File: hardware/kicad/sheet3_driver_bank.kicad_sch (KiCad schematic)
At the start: 32 parts, among them U101 TC4427ACOA, U102 TC4427ACOA, U103 TC4427ACOA, U104 TC4427ACOA, U105 TC4427ACOA, U106 TC4427ACOA, U107 TC4427ACOA, U108 TC4427ACOA, U109 TC4427ACOA, U110 TC4427ACOA, U111 TC4427ACOA, U112 TC4427ACOA, U113 TC4427ACOA, U114 TC4427ACOA, U115 TC4427ACOA, U116 TC4427ACOA, U117 TC4427ACOA, U118 TC4427ACOA, U119 TC4427ACOA, U120 TC4427ACOA, U121 TC4427ACOA, U122 TC4427ACOA, U123 TC4427ACOA, U124 TC4427ACOA, U125 TC4427ACOA, U126 TC4427ACOA, U127 TC4427ACOA, U128 TC4427ACOA, U129 TC4427ACOA, U130 TC4427ACOA, U131 TC4427ACOA, U132 TC4427ACOA

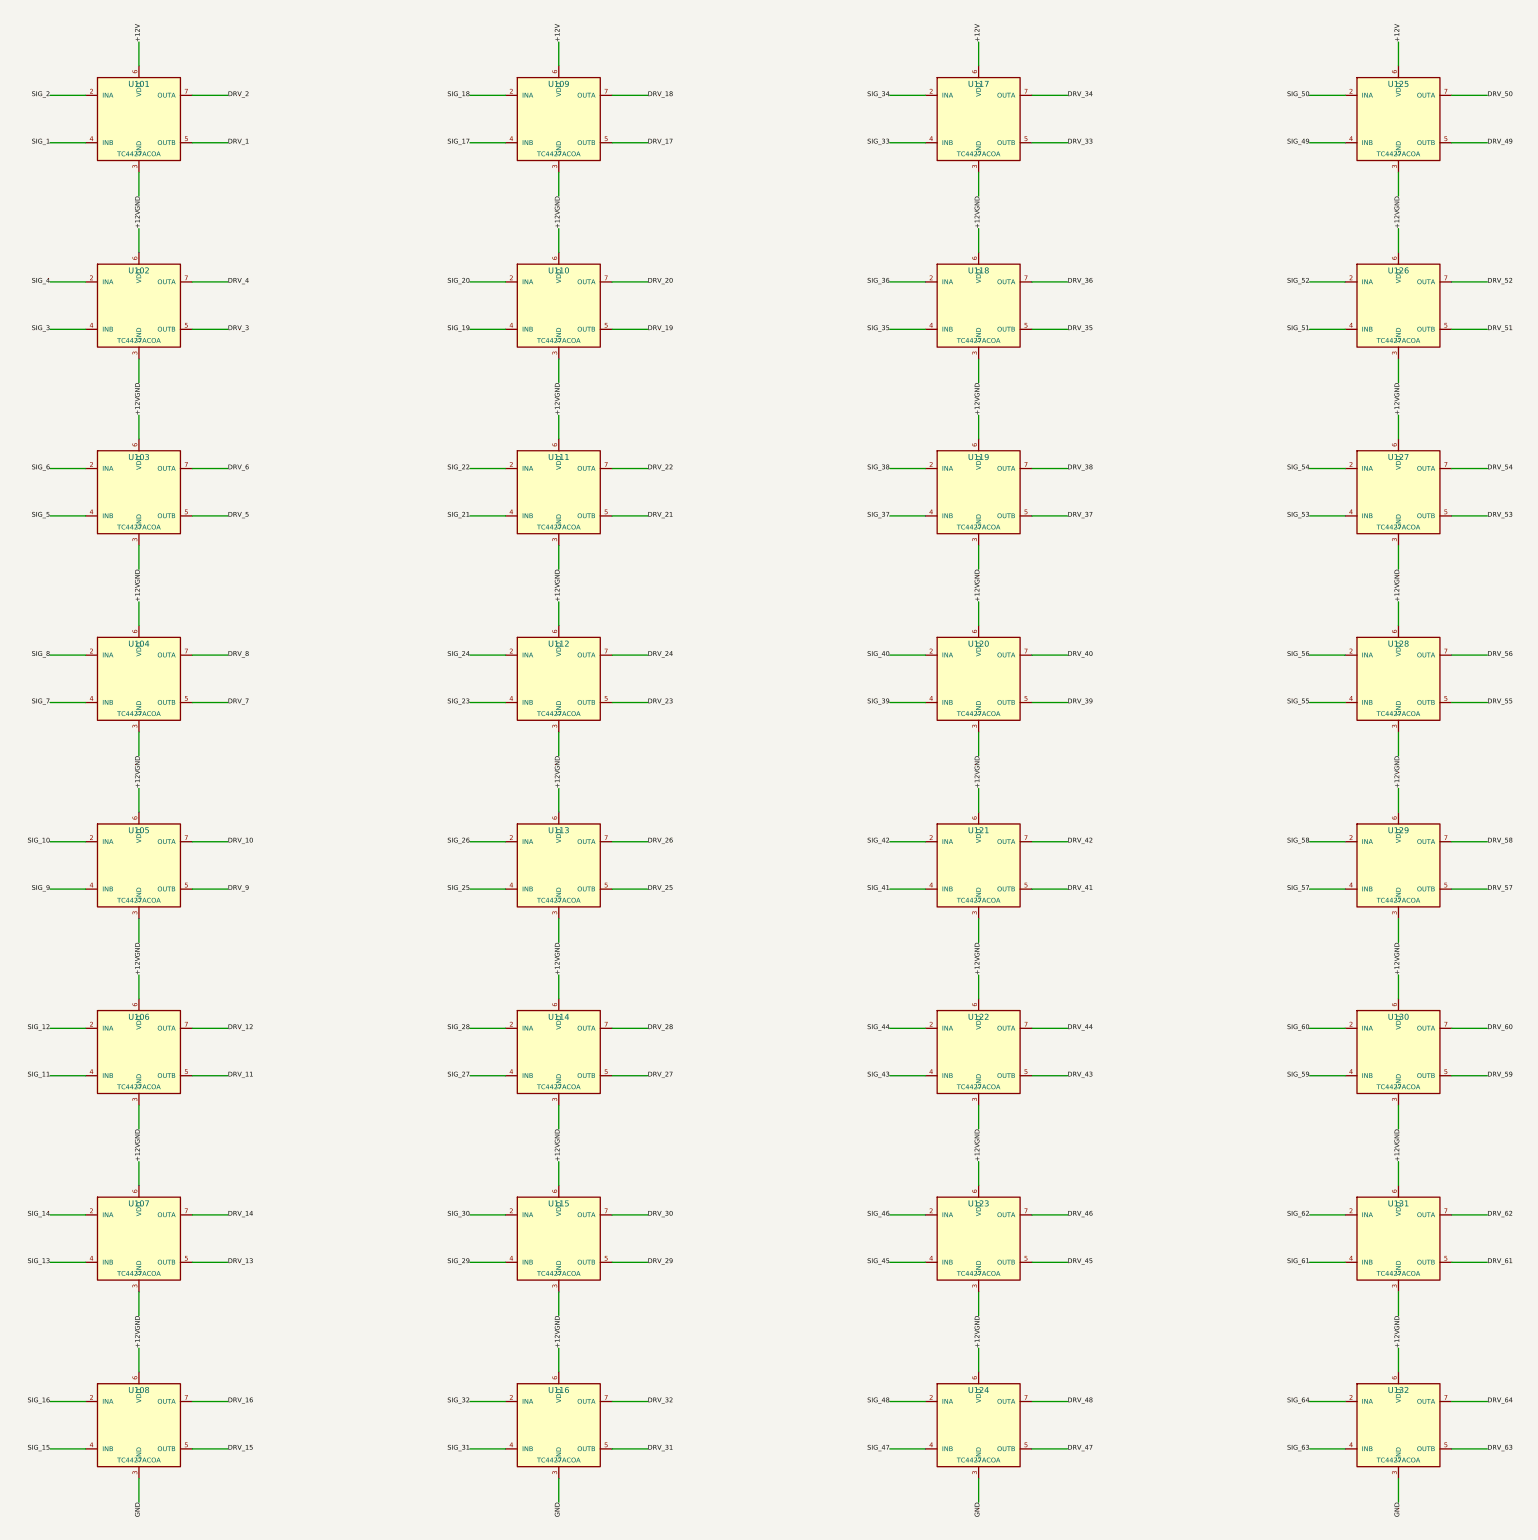
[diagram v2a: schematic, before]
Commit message: Update KiCad symbols and netlist for spotless F8 PCB sync
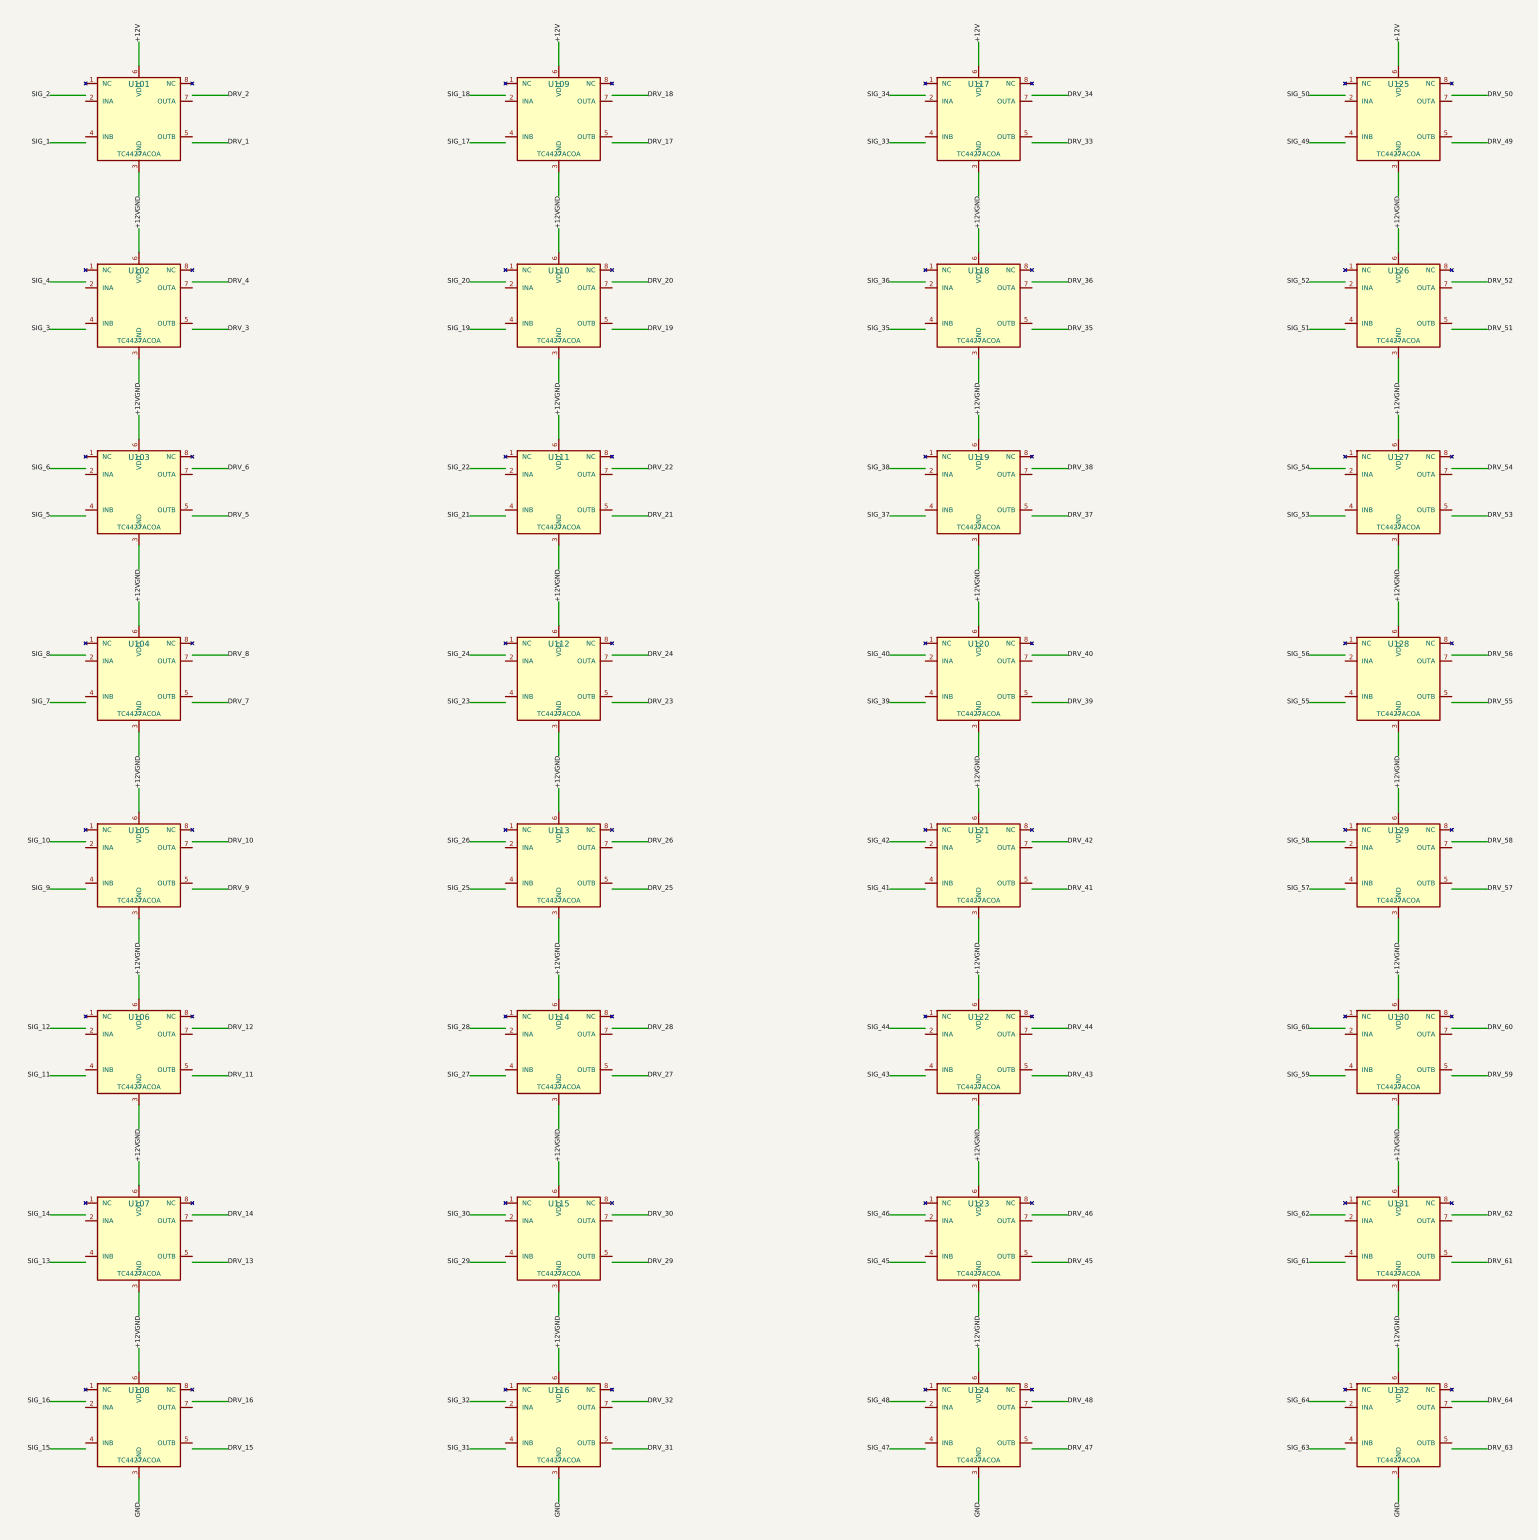
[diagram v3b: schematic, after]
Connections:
- net DRV_1: no longer U101.5 (OUTB)
- net DRV_10: no longer U105.7 (OUTA)
- net DRV_11: no longer U106.5 (OUTB)
- net DRV_12: no longer U106.7 (OUTA)
- net DRV_13: no longer U107.5 (OUTB)
- net DRV_14: no longer U107.7 (OUTA)
- net DRV_15: no longer U108.5 (OUTB)
- net DRV_16: no longer U108.7 (OUTA)
- net DRV_17: no longer U109.5 (OUTB)
- net DRV_18: no longer U109.7 (OUTA)
- net DRV_19: no longer U110.5 (OUTB)
- net DRV_2: no longer U101.7 (OUTA)
- net DRV_20: no longer U110.7 (OUTA)
- net DRV_21: no longer U111.5 (OUTB)
- net DRV_22: no longer U111.7 (OUTA)
- net DRV_23: no longer U112.5 (OUTB)
- net DRV_24: no longer U112.7 (OUTA)
- net DRV_25: no longer U113.5 (OUTB)
- net DRV_26: no longer U113.7 (OUTA)
- net DRV_27: no longer U114.5 (OUTB)
- net DRV_28: no longer U114.7 (OUTA)
- net DRV_29: no longer U115.5 (OUTB)
- net DRV_3: no longer U102.5 (OUTB)
- net DRV_30: no longer U115.7 (OUTA)
- net DRV_31: no longer U116.5 (OUTB)
- net DRV_32: no longer U116.7 (OUTA)
- net DRV_33: no longer U117.5 (OUTB)
- net DRV_34: no longer U117.7 (OUTA)
- net DRV_35: no longer U118.5 (OUTB)
- net DRV_36: no longer U118.7 (OUTA)
- net DRV_37: no longer U119.5 (OUTB)
- net DRV_38: no longer U119.7 (OUTA)
- net DRV_39: no longer U120.5 (OUTB)
- net DRV_4: no longer U102.7 (OUTA)
- net DRV_40: no longer U120.7 (OUTA)
- net DRV_41: no longer U121.5 (OUTB)
- net DRV_42: no longer U121.7 (OUTA)
- net DRV_43: no longer U122.5 (OUTB)
- net DRV_44: no longer U122.7 (OUTA)
- net DRV_45: no longer U123.5 (OUTB)
- net DRV_46: no longer U123.7 (OUTA)
- net DRV_47: no longer U124.5 (OUTB)
- net DRV_48: no longer U124.7 (OUTA)
- net DRV_49: no longer U125.5 (OUTB)
- net DRV_5: no longer U103.5 (OUTB)
- net DRV_50: no longer U125.7 (OUTA)
- net DRV_51: no longer U126.5 (OUTB)
- net DRV_52: no longer U126.7 (OUTA)
- net DRV_53: no longer U127.5 (OUTB)
- net DRV_54: no longer U127.7 (OUTA)
- net DRV_55: no longer U128.5 (OUTB)
- net DRV_56: no longer U128.7 (OUTA)
- net DRV_57: no longer U129.5 (OUTB)
- net DRV_58: no longer U129.7 (OUTA)
- net DRV_59: no longer U130.5 (OUTB)
- net DRV_6: no longer U103.7 (OUTA)
- net DRV_60: no longer U130.7 (OUTA)
- net DRV_61: no longer U131.5 (OUTB)
- net DRV_62: no longer U131.7 (OUTA)
- net DRV_63: no longer U132.5 (OUTB)
- net DRV_64: no longer U132.7 (OUTA)
- net DRV_7: no longer U104.5 (OUTB)
- net DRV_8: no longer U104.7 (OUTA)
- net DRV_9: no longer U105.5 (OUTB)
- net SIG_1: no longer U101.4 (INB)
- net SIG_10: no longer U105.2 (INA)
- net SIG_11: no longer U106.4 (INB)
- net SIG_12: no longer U106.2 (INA)
- net SIG_13: no longer U107.4 (INB)
- net SIG_14: no longer U107.2 (INA)
- net SIG_15: no longer U108.4 (INB)
- net SIG_16: no longer U108.2 (INA)
- net SIG_17: no longer U109.4 (INB)
- net SIG_18: no longer U109.2 (INA)
- net SIG_19: no longer U110.4 (INB)
- net SIG_2: no longer U101.2 (INA)
- net SIG_20: no longer U110.2 (INA)
- net SIG_21: no longer U111.4 (INB)
- net SIG_22: no longer U111.2 (INA)
- net SIG_23: no longer U112.4 (INB)
- net SIG_24: no longer U112.2 (INA)
- net SIG_25: no longer U113.4 (INB)
- net SIG_26: no longer U113.2 (INA)
- net SIG_27: no longer U114.4 (INB)
- net SIG_28: no longer U114.2 (INA)
- net SIG_29: no longer U115.4 (INB)
- net SIG_3: no longer U102.4 (INB)
- net SIG_30: no longer U115.2 (INA)
- net SIG_31: no longer U116.4 (INB)
- net SIG_32: no longer U116.2 (INA)
- net SIG_33: no longer U117.4 (INB)
- net SIG_34: no longer U117.2 (INA)
- net SIG_35: no longer U118.4 (INB)
- net SIG_36: no longer U118.2 (INA)
- net SIG_37: no longer U119.4 (INB)
- net SIG_38: no longer U119.2 (INA)
- net SIG_39: no longer U120.4 (INB)
- net SIG_4: no longer U102.2 (INA)
- net SIG_40: no longer U120.2 (INA)
- net SIG_41: no longer U121.4 (INB)
- net SIG_42: no longer U121.2 (INA)
- net SIG_43: no longer U122.4 (INB)
- net SIG_44: no longer U122.2 (INA)
- net SIG_45: no longer U123.4 (INB)
- net SIG_46: no longer U123.2 (INA)
- net SIG_47: no longer U124.4 (INB)
- net SIG_48: no longer U124.2 (INA)
- net SIG_49: no longer U125.4 (INB)
- net SIG_5: no longer U103.4 (INB)
- net SIG_50: no longer U125.2 (INA)
- net SIG_51: no longer U126.4 (INB)
- net SIG_52: no longer U126.2 (INA)
- net SIG_53: no longer U127.4 (INB)
- net SIG_54: no longer U127.2 (INA)
- net SIG_55: no longer U128.4 (INB)
- net SIG_56: no longer U128.2 (INA)
- net SIG_57: no longer U129.4 (INB)
- net SIG_58: no longer U129.2 (INA)
- net SIG_59: no longer U130.4 (INB)
- net SIG_6: no longer U103.2 (INA)
- net SIG_60: no longer U130.2 (INA)
- net SIG_61: no longer U131.4 (INB)
- net SIG_62: no longer U131.2 (INA)
- net SIG_63: no longer U132.4 (INB)
- net SIG_64: no longer U132.2 (INA)
- net SIG_7: no longer U104.4 (INB)
- net SIG_8: no longer U104.2 (INA)
- net SIG_9: no longer U105.4 (INB)
